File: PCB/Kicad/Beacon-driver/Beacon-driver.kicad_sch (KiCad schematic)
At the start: 8 parts, among them IC1 AL8860MP-13, J1 Conn_01x01_Female, J2 Conn_01x01_Female

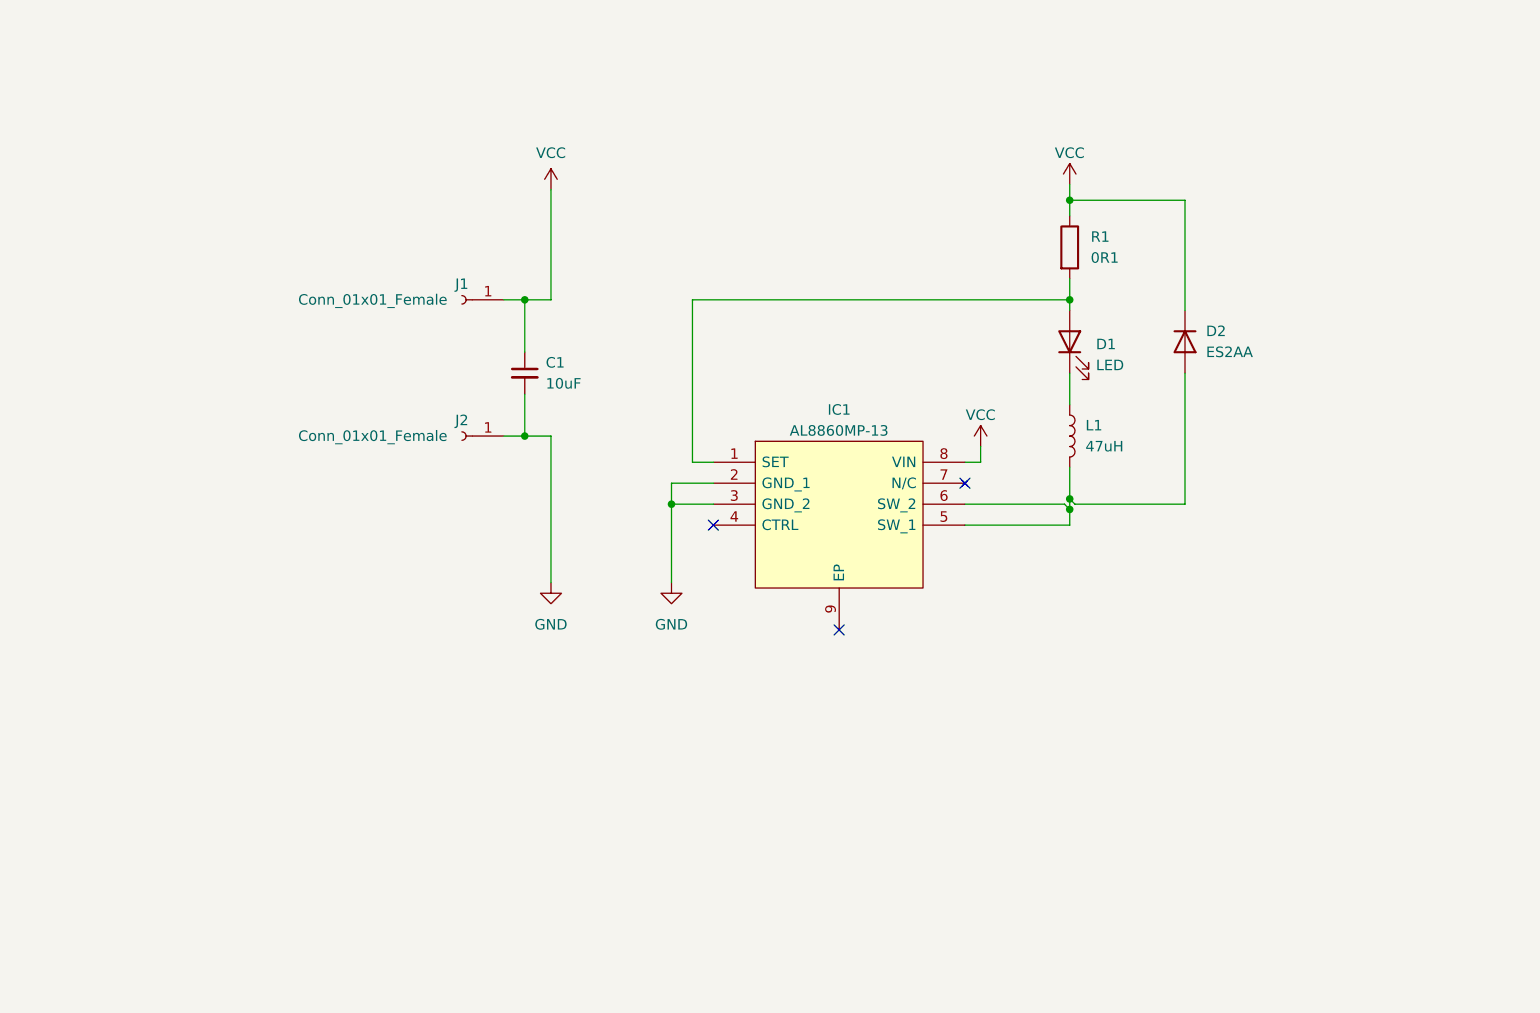
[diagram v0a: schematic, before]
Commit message: Add Beacon schematic and PCB design
Add Kicad files for the schematic and PCB of the beacon circuit
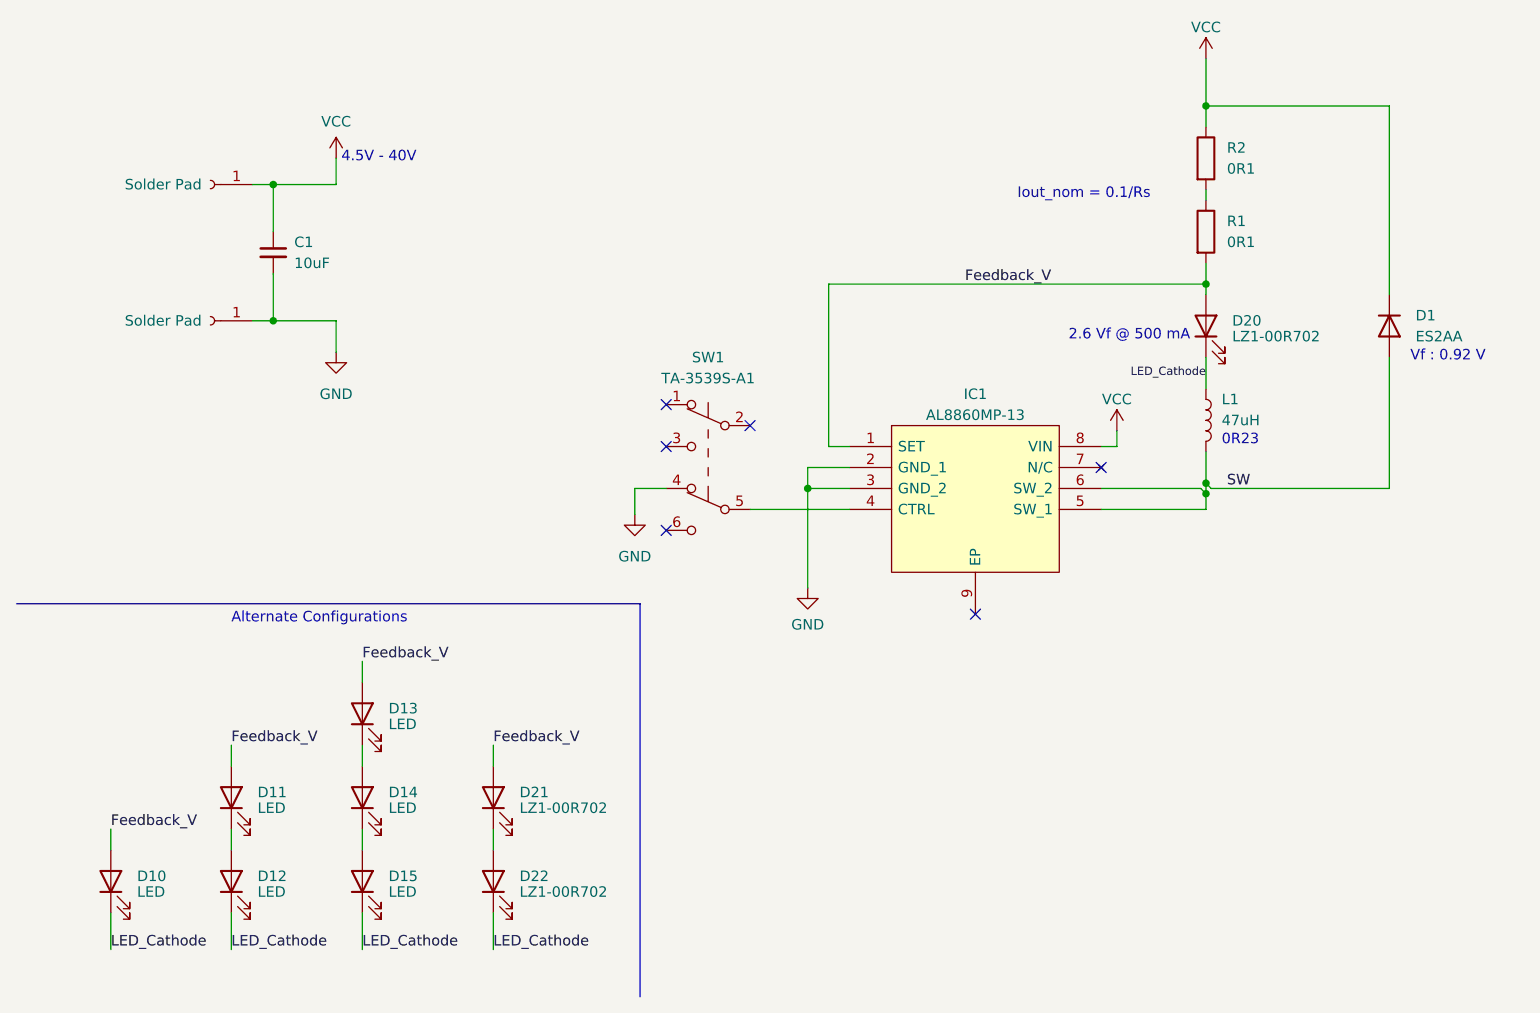
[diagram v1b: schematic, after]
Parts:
- added D10, D11, D12, D13, D14, D15: LED, KiCad:SE03-EMC3838A-C90-940 (jank led), symbol Device:LED
- added D21, D22: LZ1-00R702, KiCad:LZ1-00R702, symbol Device:LED
- added R2: 0R1, Resistor_SMD:R_0805_2012Metric, symbol Device:R
- added SW1: TA-3539S-A1, KiCad:TA-3539S-A1 switch, symbol Switch:SW_Push_DPDT
- C1: footprint (none) -> Capacitor_SMD:C_0603_1608Metric
- D1: renamed from D2; footprint (none) -> Diode_SMD:D_SMA
- D20: renamed from D1; value LED -> LZ1-00R702; footprint (none) -> KiCad:LZ1-00R702
- IC1: footprint SOP65P490X110-9N -> Package_SO:MSOP-8-1EP_3x3mm_P0.65mm_EP1.68x1.88mm
- J1, J2: value Conn_01x01_Female -> Solder Pad
- L1: footprint (none) -> KiCad:VLS-EX-H
- R1: footprint (none) -> Resistor_SMD:R_0805_2012Metric
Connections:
- net GND: now also SW1.4 (A)
- net VCC: now also R2.1; no longer R1.1
- net LED_Cathode: now reaches D20.1 (K), L1.1
- net LED_Cathode: now also D10.1 (K), D12.1 (K), D15.1 (K), D22.1 (K)
- net Feedback_V: now reaches D20.2 (A), IC1.1 (SET), R1.2
- net Feedback_V: now also D10.2 (A), D11.2 (A), D13.2 (A), D21.2 (A)
- net SW: now reaches D1.2 (A), IC1.5 (SW_1), IC1.6 (SW_2), L1.2
- net at IC1.4 (CTRL): now also SW1.5 (B)
- new net: D14.1 (K), D15.2 (A)
- new net: D21.1 (K), D22.2 (A)
- new net: R1.1, R2.2
- new net: D13.1 (K), D14.2 (A)
- new net: D11.1 (K), D12.2 (A)
- no-connect marks 3 -> 6
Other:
- note added: "0R23"
- note added: "2.6 Vf @ 500 mA"
- note added: "4.5V - 40V"
- note added: "Alternate Configurations"
- note added: "Iout_nom = 0.1/Rs"
- note added: "Vf : 0.92 V"
- title: (none) -> Oreo IR Beacon Board
- moved on the sheet: C1, D1, D20, IC1, L1, R1
